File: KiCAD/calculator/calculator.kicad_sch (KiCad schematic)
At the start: 43 parts, among them SW1 2nd, SW10 x^2, SW11 EE, SW12 7, SW13 (, SW14 8, SW15 ), SW16 9, SW17 log_10, SW18 ln, SW19 del, SW2 DRG, SW20 5, SW21 1, SW22 0, SW23 6, SW24 2, SW25 ., SW26 7, SW27 3, SW28 +/-, SW29 x, SW3 C, SW30 -, SW31 +, SW32 =, SW33 1/x, SW4 Pi, SW5 sin, SW6 cos, SW7 tan, SW8 ÷, SW9 y^x, U1 STM32G031K8T6

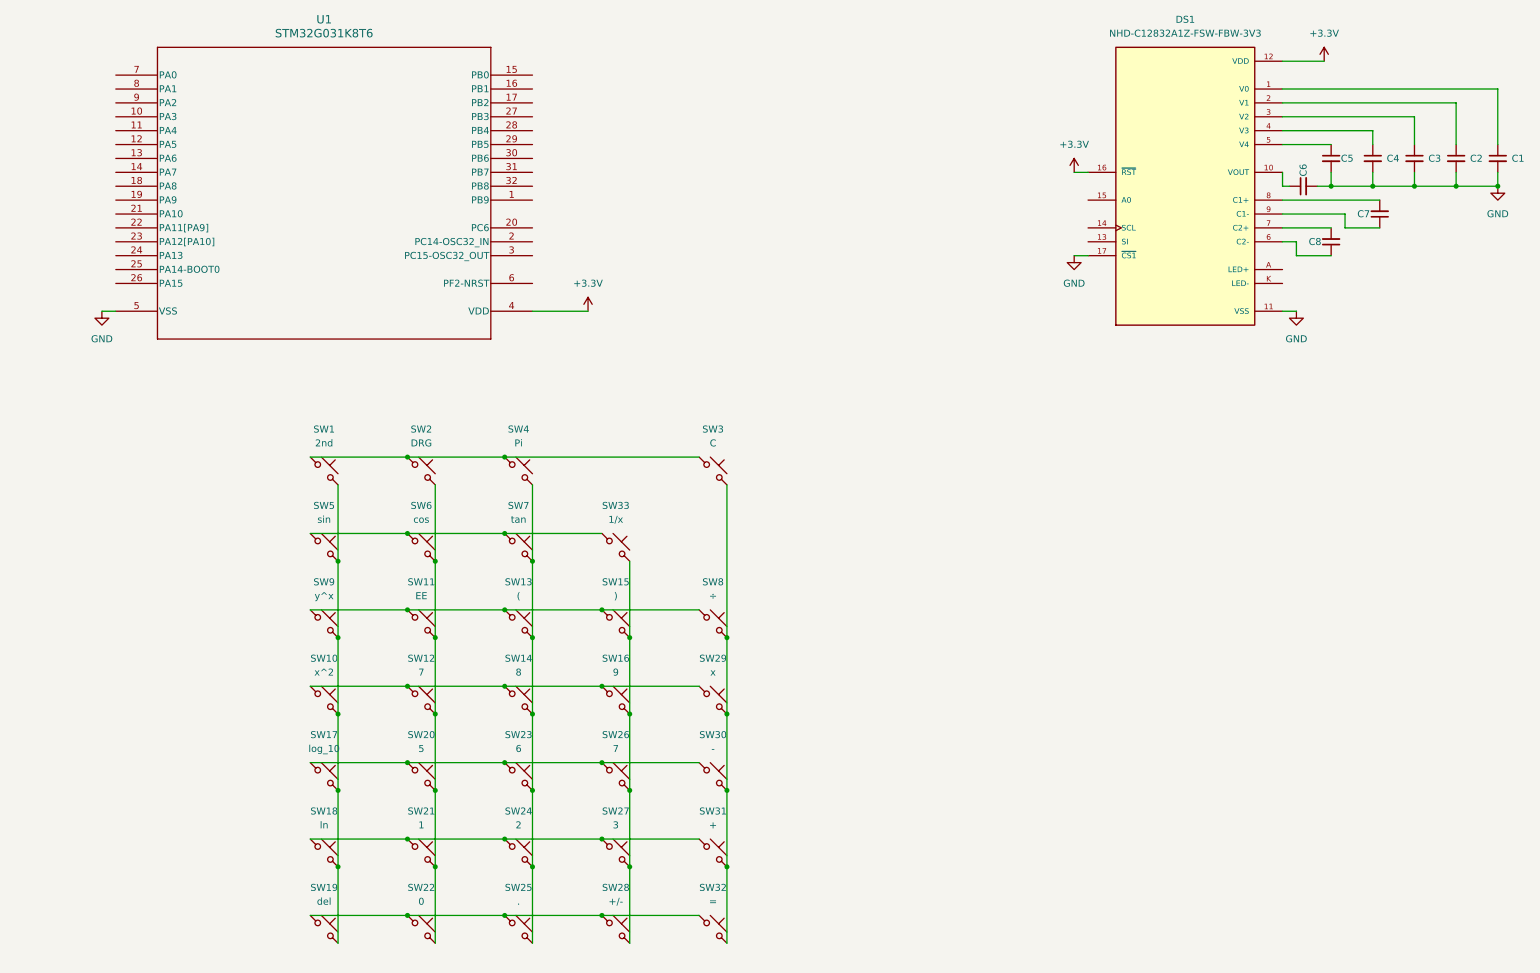
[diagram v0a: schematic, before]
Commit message: Re-arrange KiCAD schematic
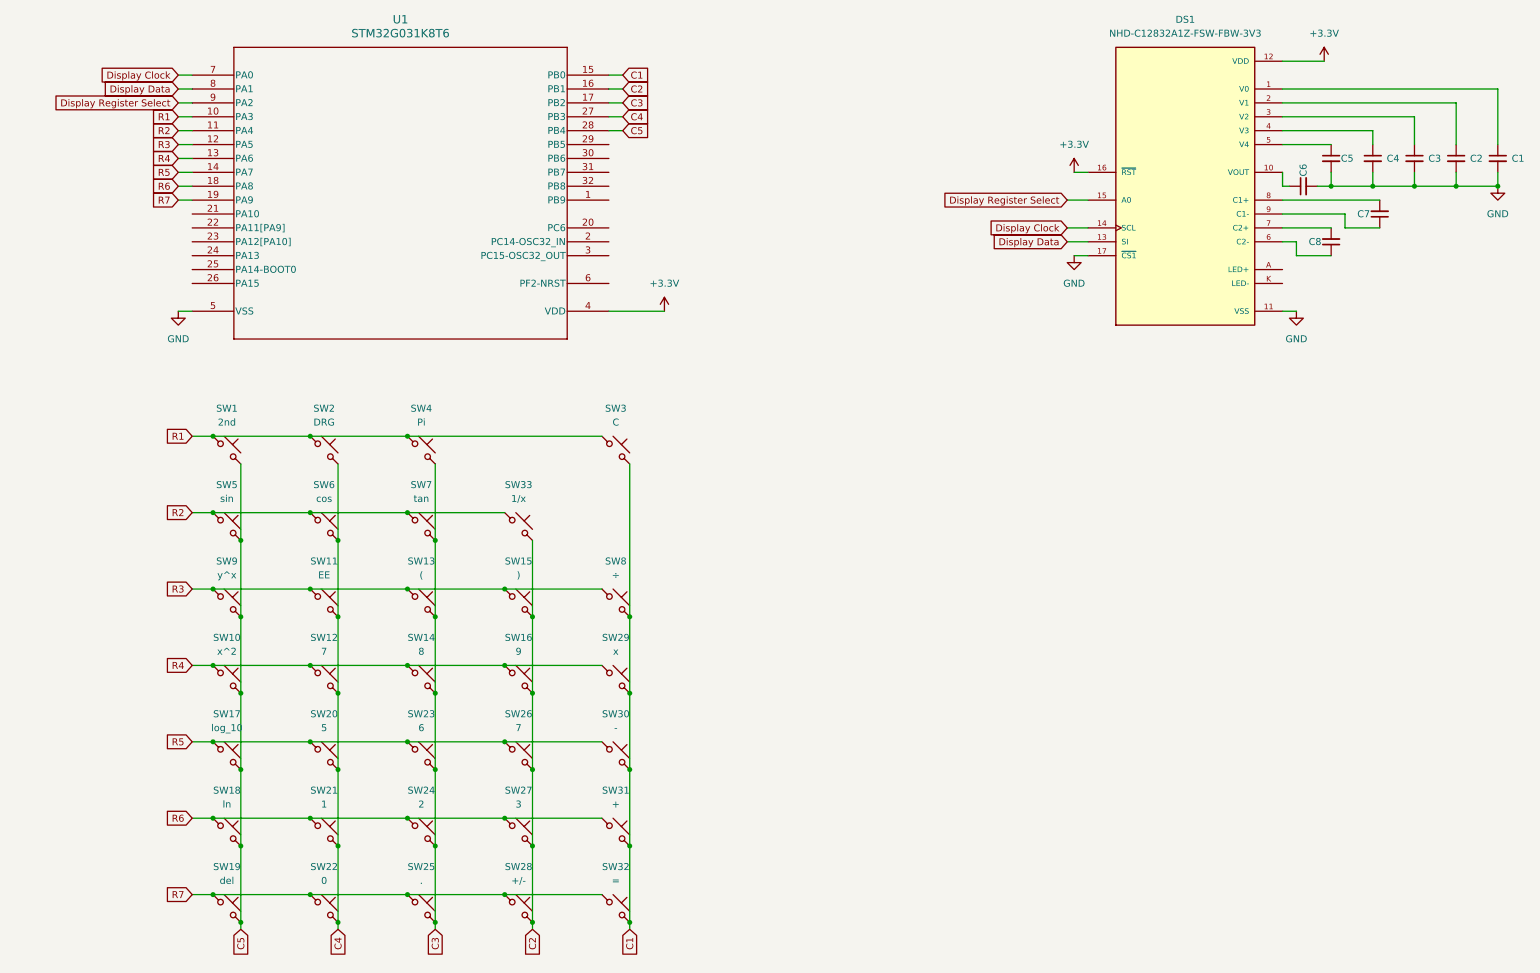
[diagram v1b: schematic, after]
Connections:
- net R3: now reaches SW11.1, SW13.1, SW15.1, SW8.1, SW9.1
- net R3: now also U1.12 (PA5)
- net C2: now reaches SW15.2, SW16.2, SW26.2, SW27.2, SW28.2, SW33.2
- net C2: now also U1.16 (PB1)
- net R7: now reaches SW19.1, SW22.1, SW25.1, SW28.1, SW32.1
- net R7: now also U1.19 (PA9)
- net R4: now reaches SW10.1, SW12.1, SW14.1, SW16.1, SW29.1
- net R4: now also U1.13 (PA6)
- net C5: now reaches SW1.2, SW10.2, SW17.2, SW18.2, SW19.2, SW5.2, SW9.2
- net C5: now also U1.28 (PB4)
- net R5: now reaches SW17.1, SW20.1, SW23.1, SW26.1, SW30.1
- net R5: now also U1.14 (PA7)
- net C3: now reaches SW13.2, SW14.2, SW23.2, SW24.2, SW25.2, SW4.2, SW7.2
- net C3: now also U1.17 (PB2)
- net C1: now reaches SW29.2, SW3.2, SW30.2, SW31.2, SW32.2, SW8.2
- net C1: now also U1.15 (PB0)
- net R2: now reaches SW33.1, SW5.1, SW6.1, SW7.1
- net R2: now also U1.11 (PA4)
- net R1: now reaches SW1.1, SW2.1, SW3.1, SW4.1
- net R1: now also U1.10 (PA3)
- net C4: now reaches SW11.2, SW12.2, SW2.2, SW20.2, SW21.2, SW22.2, SW6.2
- net C4: now also U1.27 (PB3)
- net Display Data: now reaches DS1.13 (SI)
- net Display Data: now also U1.8 (PA1)
- net Display Clock: now reaches DS1.14 (SCL)
- net Display Clock: now also U1.7 (PA0)
- net Display Register Select: now reaches DS1.15 (A0)
- net Display Register Select: now also U1.9 (PA2)
- net R6: now reaches SW18.1, SW21.1, SW24.1, SW27.1, SW31.1
- net R6: now also U1.18 (PA8)
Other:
- moved on the sheet: SW1, SW10, SW11, SW12, SW13, SW14, SW15, SW16, SW17, SW18, SW19, SW2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
